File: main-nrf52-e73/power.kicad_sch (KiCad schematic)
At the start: 22 parts, among them J7 LTE_POWER, M1 AP2311, M2 AP2311, SW1 SW_Reed, U8 MIC5504-3.3YM5

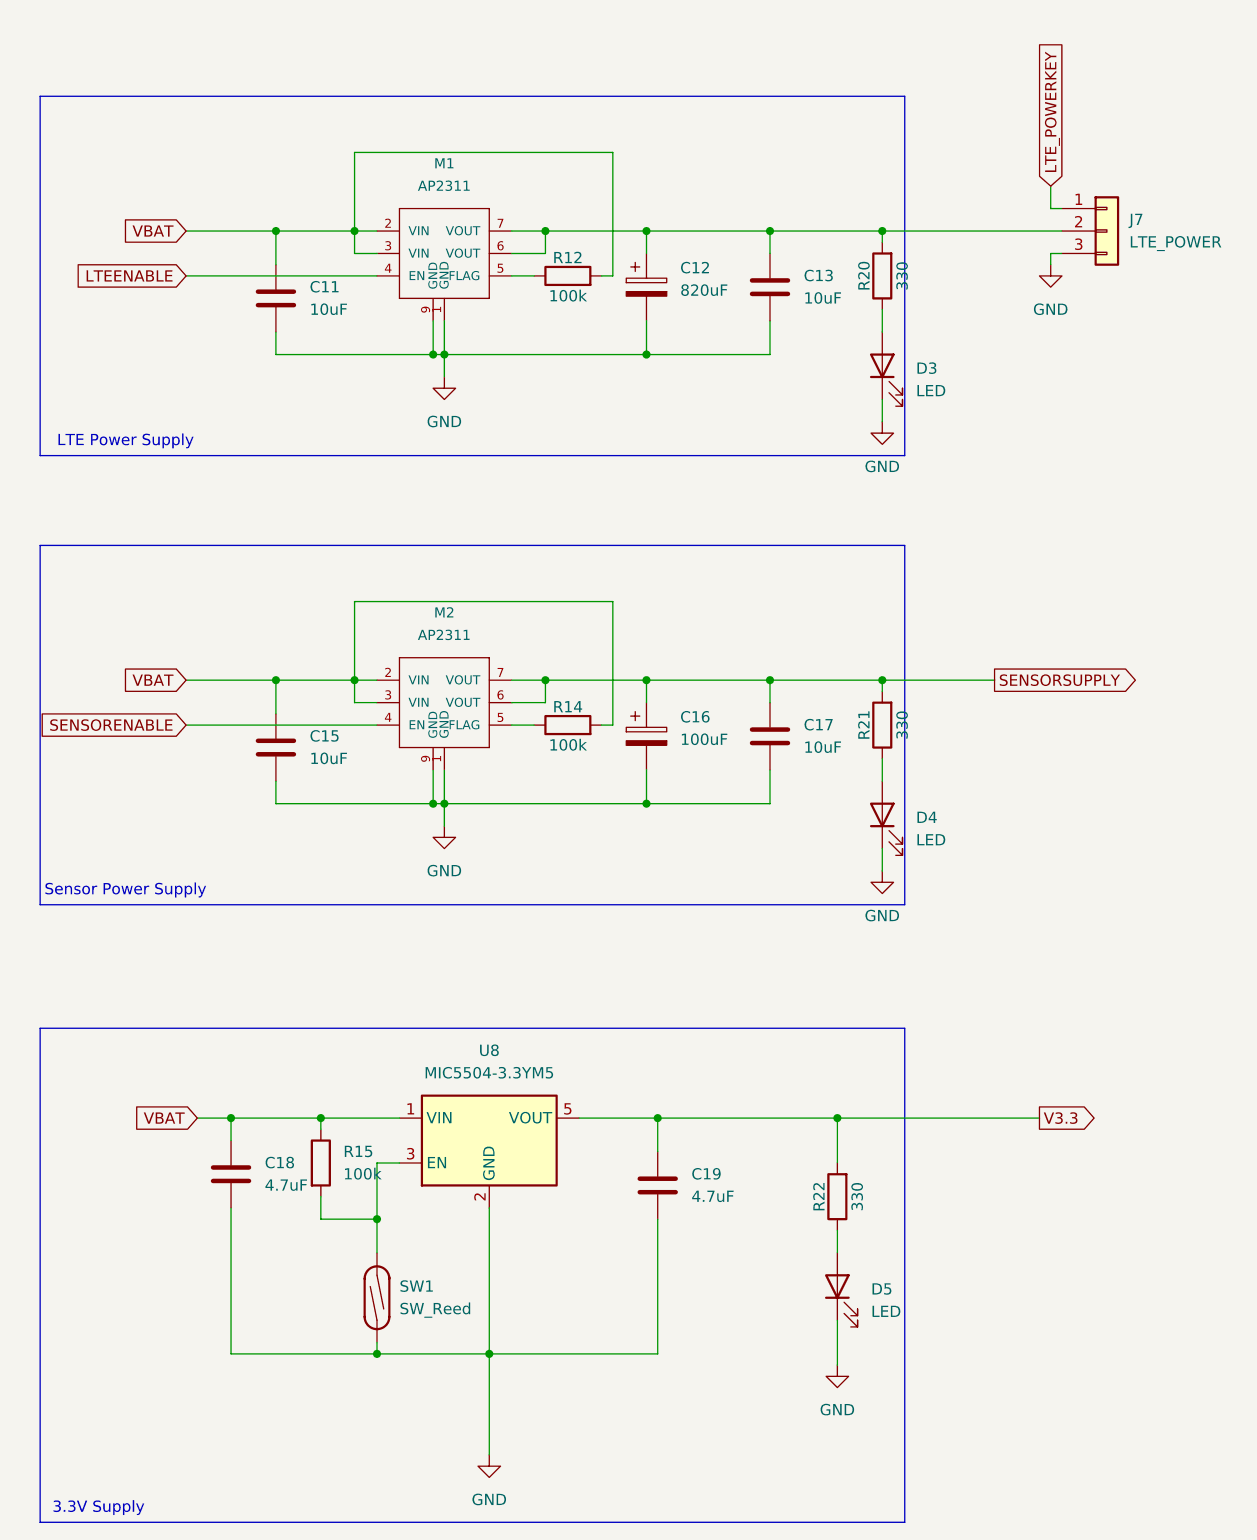
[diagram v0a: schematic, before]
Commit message: Finished first prototype of nRF52 powered main PCB.
Using Ebyte E73 module for the nRF chip.
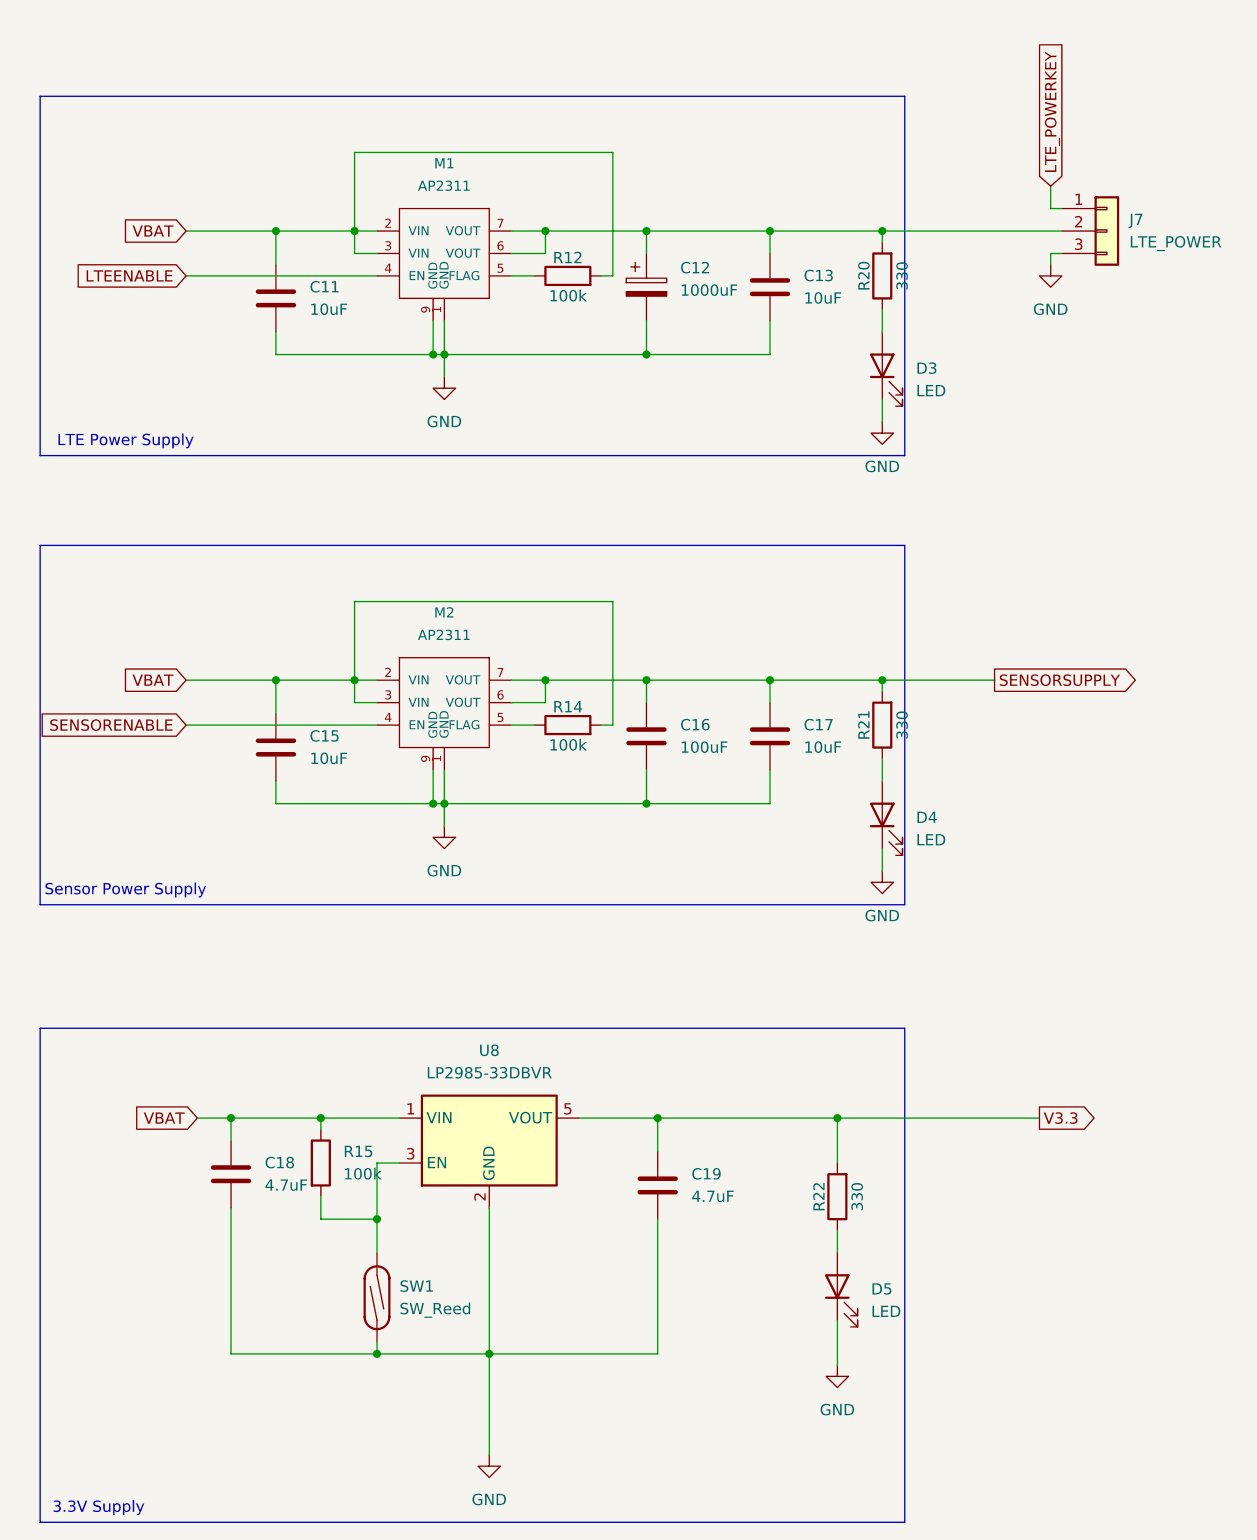
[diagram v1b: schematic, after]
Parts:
- C11, C13, C15, C17: LCSC (none) -> C15850
- C12: value 820uF -> 1000uF; footprint Capacitor_SMD:CP_Elec_6.3x9.9 -> Capacitor_SMD:CP_Elec_10x10.5; LCSC (none) -> C263979
- C16: footprint Capacitor_SMD:C_1210_3225Metric -> Capacitor_SMD:C_1206_3216Metric; symbol Device:C_Polarized -> Device:C; LCSC (none) -> C15008
- C18, C19: LCSC (none) -> C1779
- D3, D4, D5: LCSC (none) -> C2286
- M1, M2: LCSC (none) -> C460351
- R12, R14, R15: LCSC (none) -> C25803
- R20, R21, R22: LCSC (none) -> C23138
- U8: value MIC5504-3.3YM5 -> LP2985-33DBVR; LCSC (none) -> C95414
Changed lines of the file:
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@@
+			)
+		)
+		(property "LCSC" "C15850"
+			(at 105.41 93.98 0)
+			(effects
+				(font
+					(size 1.27 1.27)
+				)
+				(hide yes)
 			)
 		)
@@
 			)
 		)
+		(property "LCSC" "C23138"
+			(at 113.03 146.05 0)
+			(effects
+				(font
+					(size 1.27 1.27)
+				)
+				(hide yes)
+			)
+		)
 		(pin "2"
 		)
@@
 			)
 		)
+		(property "LCSC" ""
+			(at 60.96 157.48 0)
+			(effects
+				(font
+					(size 1.27 1.27)
+				)
+				(hide yes)
+			)
+		)
 		(pin "1"
 		)
@@
 			)
 		)
+		(property "LCSC" "C25803"
+			(at 54.61 142.24 0)
+			(effects
+				(font
+					(size 1.27 1.27)
+				)
+				(hide yes)
+			)
+		)
 		(pin "1"
 		)
@@
 			)
 		)
+		(property "LCSC" "C25803"
+			(at 82.55 92.71 0)
+			(effects
+				(font
+					(size 1.27 1.27)
+				)
+				(hide yes)
+			)
+		)
 		(pin "2"
 		)
@@
 			)
 		)
+		(property "LCSC" ""
+			(at 143.51 36.83 0)
+			(effects
+				(font
+					(size 1.27 1.27)
+				)
+				(hide yes)
+			)
+		)
 		(pin "1"
 		)
@@
 			)
 		)
+		(property "LCSC" "C15850"
+			(at 49.53 44.45 0)
+			(effects
+				(font
+					(size 1.27 1.27)
+				)
+				(hide yes)
+			)
+		)
 		(pin "1"
 		)
@@
 			)
 		)
+		(property "LCSC" "C15850"
+			(at 105.41 43.18 0)
+			(effects
+				(font
+					(size 1.27 1.27)
+				)
+				(hide yes)
+			)
+		)
 		(pin "1"
 		)
@@
 	)
 	(symbol
-		(lib_id "Device:C_Polarized")
+		(lib_id "Device:C")
 		(at 91.44 93.98 0)
 		(unit 1)
@@
 		(fields_autoplaced yes)
 		(property "Reference" "C16"
-			(at 95.25 91.8209 0)
+			(at 95.25 92.7099 0)
 			(effects
 				(font
@@
 		)
 		(property "Value" "100uF"
-			(at 95.25 94.3609 0)
+			(at 95.25 95.2499 0)
 			(effects
 				(font
@@
 			)
 		)
-		(property "Footprint" "Capacitor_SMD:C_1210_3225Metric"
+		(property "Footprint" "Capacitor_SMD:C_1206_3216Metric"
 			(at 92.4052 97.79 0)
 			(effects
@@
 			)
 		)
-		(property "Description" "Polarized capacitor"
+		(property "Description" "Unpolarized capacitor"
+			(at 91.44 93.98 0)
+			(effects
+				(font
+					(size 1.27 1.27)
+				)
+				(hide yes)
+			)
+		)
+		(property "LCSC" "C15008"
 			(at 91.44 93.98 0)
 			(effects
@@
 			)
 		)
+		(property "LCSC" "C23138"
+			(at 118.11 92.71 0)
+			(effects
+				(font
+					(size 1.27 1.27)
+				)
+				(hide yes)
+			)
+		)
 		(pin "2"
 		)
@@
 			)
 		)
-		(property "Value" "820uF"
+		(property "Value" "1000uF"
 			(at 95.25 43.5609 0)
 			(effects
@@
 			)
 		)
-		(property "Footprint" "Capacitor_SMD:CP_Elec_6.3x9.9"
+		(property "Footprint" "Capacitor_SMD:CP_Elec_10x10.5"
 			(at 92.4052 46.99 0)
 			(effects
@@
 			)
 		)
+		(property "LCSC" "C263979"
+			(at 91.44 43.18 0)
+			(effects
+				(font
+					(size 1.27 1.27)
+				)
+				(hide yes)
+			)
+		)
 		(pin "2"
 		)
@@
 			)
 		)
+		(property "LCSC" "C15850"
+			(at 49.53 95.25 0)
+			(effects
+				(font
+					(size 1.27 1.27)
+				)
+				(hide yes)
+			)
+		)
 		(pin "1"
 		)
@@
 			)
 		)
+		(property "LCSC" "C23138"
+			(at 118.11 41.91 0)
+			(effects
+				(font
+					(size 1.27 1.27)
+				)
+				(hide yes)
+			)
+		)
 		(pin "2"
 		)
@@
 			)
 		)
+		(property "LCSC" "C2286"
+			(at 118.11 52.07 0)
+			(effects
+				(font
+					(size 1.27 1.27)
+				)
+				(hide yes)
+			)
+		)
 		(pin "2"
 		)
@@
 			)
 		)
+		(property "LCSC" "C460351"
+			(at 68.58 39.37 0)
+			(effects
+				(font
+					(size 1.27 1.27)
+				)
+				(hide yes)
+			)
+		)
 		(pin "1"
 		)
@@
 			)
 		)
+		(property "LCSC" "C1779"
+			(at 92.71 144.78 0)
+			(effects
+				(font
+					(size 1.27 1.27)
+				)
+				(hide yes)
+			)
+		)
 		(pin "1"
 		)
@@
 			)
 		)
+		(property "LCSC" "C25803"
+			(at 82.55 41.91 0)
+			(effects
+				(font
+					(size 1.27 1.27)
+				)
+				(hide yes)
+			)
+		)
 		(pin "2"
 		)
@@
 			)
 		)
-		(property "Value" "MIC5504-3.3YM5"
+		(property "Value" "LP2985-33DBVR"
 			(at 73.66 132.08 0)
 			(effects
@@
 			)
 		)
+		(property "LCSC" "C95414"
+			(at 73.66 139.7 0)
+			(effects
+				(font
+					(size 1.27 1.27)
+				)
+				(hide yes)
+			)
+		)
 		(pin "5"
 		)
@@
 			)
 		)
+		(property "LCSC" "C460351"
+			(at 68.58 90.17 0)
+			(effects
+				(font
+					(size 1.27 1.27)
+				)
+				(hide yes)
+			)
+		)
 		(pin "1"
 		)
@@
 			)
 		)
+		(property "LCSC" "C2286"
+			(at 113.03 156.21 0)
+			(effects
+				(font
+					(size 1.27 1.27)
+				)
+				(hide yes)
+			)
+		)
 		(pin "2"
 		)
@@
 			)
 		)
+		(property "LCSC" "C1779"
+			(at 44.45 143.51 0)
+			(effects
+				(font
+					(size 1.27 1.27)
+				)
+				(hide yes)
+			)
+		)
 		(pin "1"
 		)
@@
 			(at 118.11 102.87 0)
 			(effects
+				(font
+					(size 1.27 1.27)
+				)
+				(hide yes)
+			)
+		)
+		(property "LCSC" "C2286"
+			(at 118.11 102.87 0)
+			(effects
